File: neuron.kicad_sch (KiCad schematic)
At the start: 91 parts, among them J1 Conn_02x01, J2 Conn_02x01, J3 Conn_02x01, J4 Conn_02x03, Q1 2sk3018, Q10 2sk3018, Q11 2sk3018, Q12 2sk3018, Q2 2sk3018, Q3 2sk3018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

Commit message: Replace synaptic time constant and weight potentiometers by 22k
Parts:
- RV1, RV2, RV3: value 5k -> 22k; LCSC C128557 -> C128552
- RV4: value 20k -> 22k; LCSC C128550 -> C128552
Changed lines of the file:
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@@
       (effects (font (size 1.27 1.27)))
     )
-    (property "Value" "5k" (at 73.66 204.47 90)
+    (property "Value" "22k" (at 73.66 204.47 90)
       (effects (font (size 1.27 1.27)))
     )
@@
       (effects (font (size 1.27 1.27)) hide)
     )
-    (property "LCSC" "C128557" (at 73.66 198.12 0)
+    (property "LCSC" "C128552" (at 73.66 198.12 0)
       (effects (font (size 1.27 1.27)) hide)
     )
@@
       (effects (font (size 1.27 1.27)))
     )
-    (property "Value" "5k" (at 73.66 66.04 90)
+    (property "Value" "22k" (at 73.66 66.04 90)
       (effects (font (size 1.27 1.27)))
     )
@@
       (effects (font (size 1.27 1.27)) hide)
     )
-    (property "LCSC" "C128557" (at 73.66 59.69 0)
+    (property "LCSC" "C128552" (at 73.66 59.69 0)
       (effects (font (size 1.27 1.27)) hide)
     )
@@
       (effects (font (size 1.27 1.27)))
     )
-    (property "Value" "5k" (at 73.66 135.89 90)
+    (property "Value" "22k" (at 73.66 135.89 90)
       (effects (font (size 1.27 1.27)))
     )
@@
       (effects (font (size 1.27 1.27)) hide)
     )
-    (property "LCSC" "C128557" (at 73.66 129.54 0)
+    (property "LCSC" "C128552" (at 73.66 129.54 0)
       (effects (font (size 1.27 1.27)) hide)
     )
@@
       (effects (font (size 1.27 1.27)) (justify right))
     )
-    (property "Value" "20k" (at 125.73 85.725 0)
+    (property "Value" "22k" (at 125.73 85.725 0)
       (effects (font (size 1.27 1.27)) (justify right))
     )
@@
       (effects (font (size 1.27 1.27)) hide)
     )
-    (property "LCSC" "C128550" (at 127.635 83.185 0)
+    (property "LCSC" "C128552" (at 127.635 83.185 0)
       (effects (font (size 1.27 1.27)) hide)
     )

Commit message: Replace membrane capacitor by more common part
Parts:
- C5: LCSC C2836678 -> C415703
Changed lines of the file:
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@@
       (effects (font (size 1.27 1.27)) hide)
     )
-    (property "LCSC" "C2836678" (at 232.41 98.425 0)
+    (property "LCSC" "C415703" (at 232.41 98.425 0)
       (effects (font (size 1.27 1.27)) hide)
     )

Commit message: Replace LEDs by more yellow one
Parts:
- D1, D2, D3, D4, D5, D6, D7: LCSC C779448 -> C965792
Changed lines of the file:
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@@
       (effects (font (size 1.27 1.27)) hide)
     )
-    (property "LCSC" "C779448" (at 401.32 104.775 0)
+    (property "LCSC" "C965792" (at 401.32 104.775 0)
       (effects (font (size 1.27 1.27)) hide)
     )
@@
       (effects (font (size 1.27 1.27)) hide)
     )
-    (property "LCSC" "C779448" (at 401.32 117.475 0)
+    (property "LCSC" "C965792" (at 401.32 117.475 0)
       (effects (font (size 1.27 1.27)) hide)
     )
@@
       (effects (font (size 1.27 1.27)) hide)
     )
-    (property "LCSC" "C779448" (at 401.32 66.675 0)
+    (property "LCSC" "C965792" (at 401.32 66.675 0)
       (effects (font (size 1.27 1.27)) hide)
     )
@@
       (effects (font (size 1.27 1.27)) hide)
     )
-    (property "LCSC" "C779448" (at 401.32 130.175 0)
+    (property "LCSC" "C965792" (at 401.32 130.175 0)
       (effects (font (size 1.27 1.27)) hide)
     )
@@
       (effects (font (size 1.27 1.27)) hide)
     )
-    (property "LCSC" "C779448" (at 401.32 92.075 0)
+    (property "LCSC" "C965792" (at 401.32 92.075 0)
       (effects (font (size 1.27 1.27)) hide)
     )
@@
       (effects (font (size 1.27 1.27)) hide)
     )
-    (property "LCSC" "C779448" (at 400.05 151.13 0)
+    (property "LCSC" "C965792" (at 400.05 151.13 0)
       (effects (font (size 1.27 1.27)) hide)
     )
@@
       (effects (font (size 1.27 1.27)) hide)
     )
-    (property "LCSC" "C779448" (at 401.32 79.375 0)
-      (effects (font (size 1.27 1.27)) hide)
-    )
+    (property "LCSC" "C965792" (at 401.32 79.375 0)
+      (effects (font (size 1.27 1.27)) hide)
+    )

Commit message: Change LEDs due to stock shortages
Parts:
- D1, D2, D3, D4, D5, D6, D7: LCSC C965792 -> C779450
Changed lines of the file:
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@@
       (effects (font (size 1.27 1.27)) hide)
     )
-    (property "LCSC" "C965792" (at 401.32 104.775 0)
+    (property "LCSC" "C779450" (at 401.32 104.775 0)
       (effects (font (size 1.27 1.27)) hide)
     )
@@
       (effects (font (size 1.27 1.27)) hide)
     )
-    (property "LCSC" "C965792" (at 401.32 117.475 0)
+    (property "LCSC" "C779450" (at 401.32 117.475 0)
       (effects (font (size 1.27 1.27)) hide)
     )
@@
       (effects (font (size 1.27 1.27)) hide)
     )
-    (property "LCSC" "C965792" (at 401.32 66.675 0)
+    (property "LCSC" "C779450" (at 401.32 66.675 0)
       (effects (font (size 1.27 1.27)) hide)
     )
@@
       (effects (font (size 1.27 1.27)) hide)
     )
-    (property "LCSC" "C965792" (at 401.32 130.175 0)
+    (property "LCSC" "C779450" (at 401.32 130.175 0)
       (effects (font (size 1.27 1.27)) hide)
     )
@@
       (effects (font (size 1.27 1.27)) hide)
     )
-    (property "LCSC" "C965792" (at 401.32 92.075 0)
+    (property "LCSC" "C779450" (at 401.32 92.075 0)
       (effects (font (size 1.27 1.27)) hide)
     )
@@
       (effects (font (size 1.27 1.27)) hide)
     )
-    (property "LCSC" "C965792" (at 400.05 151.13 0)
+    (property "LCSC" "C779450" (at 400.05 151.13 0)
       (effects (font (size 1.27 1.27)) hide)
     )
@@
       (effects (font (size 1.27 1.27)) hide)
     )
-    (property "LCSC" "C965792" (at 401.32 79.375 0)
-      (effects (font (size 1.27 1.27)) hide)
-    )
+    (property "LCSC" "C779450" (at 401.32 79.375 0)
+      (effects (font (size 1.27 1.27)) hide)
+    )

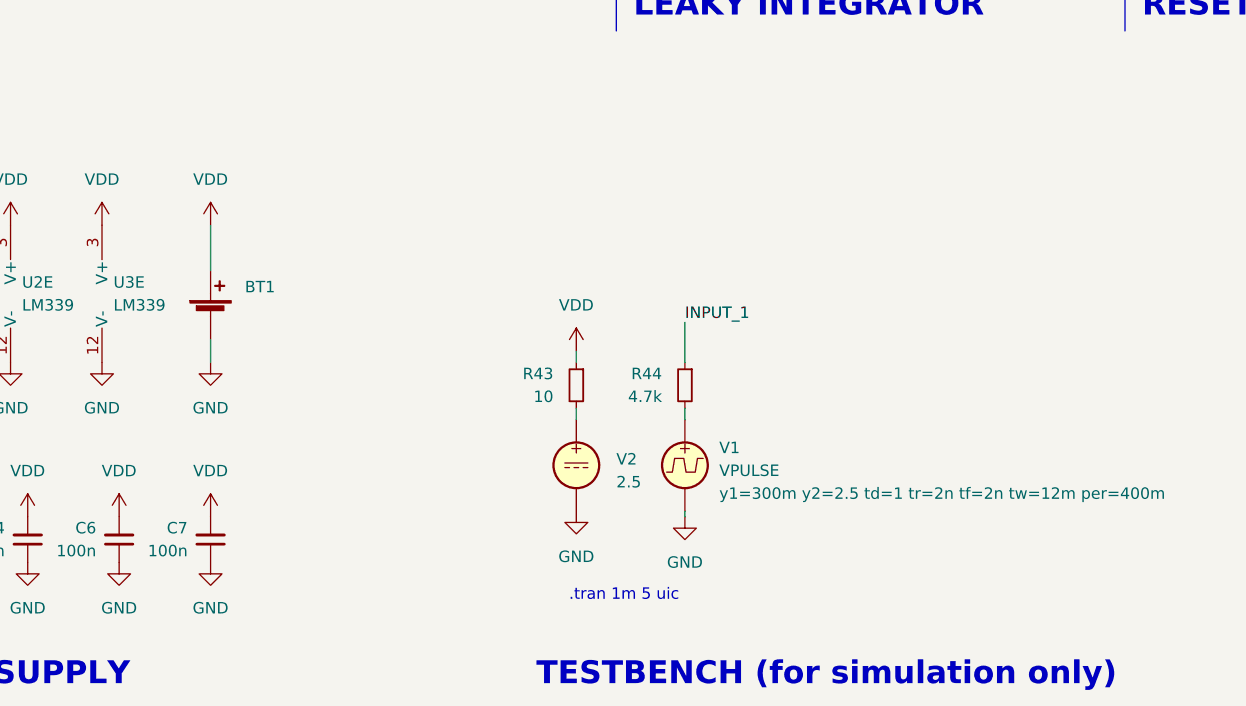
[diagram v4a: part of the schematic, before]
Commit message: Add (optional) power switch on back side
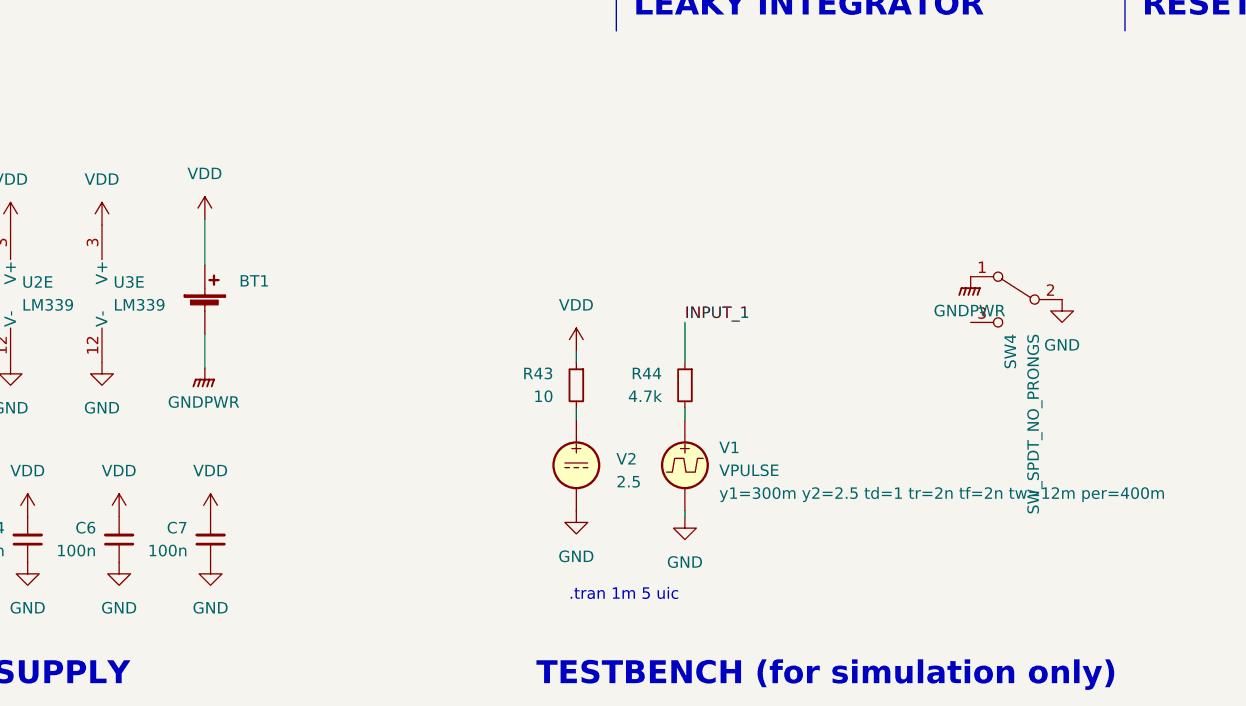
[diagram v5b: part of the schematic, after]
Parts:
- added SW4: SW_SPDT_NO_PRONGS, Custom:SSAJ120100, symbol Switch:SW_SPDT
- SW1, SW2, SW3: footprint Custom:K3-1290S-E1 -> Custom:K3-1296S-E1; LCSC C145854 -> C128955
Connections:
- net GND: now also SW4.2 (B); no longer BT1.2 (-)
- new net GNDPWR: BT1.2 (-), SW4.1 (A)
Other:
- moved on the sheet: BT1
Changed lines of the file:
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@@
     (stroke (width 0) (type default))
   )
-  (wire (pts (xy 167.005 212.725) (xy 167.005 215.265))
-    (stroke (width 0) (type default))
-  )
   (wire (pts (xy 63.5 113.03) (xy 63.5 116.84))
     (stroke (width 0) (type default))
@@
     (stroke (width 0) (type default))
   )
-  (wire (pts (xy 167.005 200.025) (xy 167.005 205.105))
+  (wire (pts (xy 166.37 199.39) (xy 166.37 204.47))
     (stroke (width 0) (type default))
   )
@@
     (stroke (width 0) (type default))
   )
+  (wire (pts (xy 166.37 212.09) (xy 166.37 215.9))
+    (stroke (width 0) (type default))
+  )
   (wire (pts (xy 367.03 107.315) (xy 369.57 107.315))
     (stroke (width 0) (type default))
@@
     )
   )
-  (symbol (lib_id "power:VDD") (at 167.005 200.025 0) (unit 1)
+  (symbol (lib_id "power:VDD") (at 166.37 199.39 0) (unit 1)
     (in_bom yes) (on_board yes) (dnp no) (fields_autoplaced)
-    (property "Reference" "#PWR023" (at 167.005 203.835 0)
+    (property "Reference" "#PWR023" (at 166.37 203.2 0)
       (effects (font (size 1.27 1.27)) hide)
     )
-    (property "Value" "VDD" (at 167.005 194.945 0)
+    (property "Value" "VDD" (at 166.37 194.31 0)
       (effects (font (size 1.27 1.27)))
     )
-    (property "Footprint" "" (at 167.005 200.025 0)
+    (property "Footprint" "" (at 166.37 199.39 0)
       (effects (font (size 1.27 1.27)) hide)
     )
-    (property "Datasheet" "" (at 167.005 200.025 0)
+    (property "Datasheet" "" (at 166.37 199.39 0)
       (effects (font (size 1.27 1.27)) hide)
     )
@@
       (effects (font (size 1.27 1.27)) (justify right))
     )
-    (property "Footprint" "Custom:K3-1290S-E1" (at 50.8 137.16 0)
+    (property "Footprint" "Custom:K3-1296S-E1" (at 50.8 137.16 0)
       (effects (font (size 1.27 1.27)) hide)
     )
@@
       (effects (font (size 1.27 1.27)) hide)
     )
-    (property "LCSC" "C145854" (at 50.8 137.16 0)
+    (property "LCSC" "C128955" (at 50.8 137.16 0)
       (effects (font (size 1.27 1.27)) hide)
     )
@@
     )
   )
+  (symbol (lib_id "power:GND") (at 261.62 208.28 0) (unit 1)
+    (in_bom yes) (on_board yes) (dnp no) (fields_autoplaced)
+    (property "Reference" "#PWR064" (at 261.62 214.63 0)
+      (effects (font (size 1.27 1.27)) hide)
+    )
+    (property "Value" "GND" (at 261.62 213.36 0)
+      (effects (font (size 1.27 1.27)))
+    )
+    (property "Footprint" "" (at 261.62 208.28 0)
+      (effects (font (size 1.27 1.27)) hide)
+    )
+    (property "Datasheet" "" (at 261.62 208.28 0)
+      (effects (font (size 1.27 1.27)) hide)
+    )
+    (pin "1")
+    (instances
+      (project "neuron"
+        (path "/ceb44bb3-3806-4f1d-b60c-2d4eb7174dea"
+          (reference "#PWR064") (unit 1)
+        )
+      )
+    )
+  )
   (symbol (lib_id "Device:C_Small") (at 337.185 115.57 0) (mirror y) (unit 1)
     (in_bom yes) (on_board yes) (dnp no)
@@
     )
   )
-  (symbol (lib_id "Device:Battery_Cell") (at 167.005 210.185 0) (unit 1)
+  (symbol (lib_id "Device:Battery_Cell") (at 166.37 209.55 0) (unit 1)
     (in_bom yes) (on_board yes) (dnp no) (fields_autoplaced)
-    (property "Reference" "BT1" (at 170.815 206.8829 0)
+    (property "Reference" "BT1" (at 170.18 206.2479 0)
       (effects (font (size 1.27 1.27)) (justify left))
     )
-    (property "Value" "type=\"R\" model=\"Battery_Cell\" lib=\"\"" (at 170.815 209.4229 0)
+    (property "Value" "type=\"R\" model=\"Battery_Cell\" lib=\"\"" (at 170.18 208.7879 0)
       (effects (font (size 1.27 1.27)) (justify left) hide)
     )
-    (property "Footprint" "Custom:CR2032_Holder" (at 167.005 208.661 90)
+    (property "Footprint" "Custom:CR2032_Holder" (at 166.37 208.026 90)
       (effects (font (size 1.27 1.27)) hide)
     )
-    (property "Datasheet" "~" (at 167.005 208.661 90)
+    (property "Datasheet" "~" (at 166.37 208.026 90)
       (effects (font (size 1.27 1.27)) hide)
     )
-    (property "LCSC" "C70377" (at 167.005 210.185 0)
+    (property "LCSC" "C70377" (at 166.37 209.55 0)
       (effects (font (size 1.27 1.27)) hide)
     )
-    (property "Sim.Enable" "0" (at 167.005 210.185 0)
+    (property "Sim.Enable" "0" (at 166.37 209.55 0)
       (effects (font (size 1.27 1.27)) hide)
     )
-    (property "Sim.Device" "SPICE" (at 167.005 210.185 0)
+    (property "Sim.Device" "SPICE" (at 166.37 209.55 0)
       (effects (font (size 1.27 1.27)) hide)
     )
-    (property "Sim.Params" "type=\"R\" model=\"Battery_Cell\" lib=\"\"" (at 73.025 29.845 0)
+    (property "Sim.Params" "type=\"R\" model=\"Battery_Cell\" lib=\"\"" (at 72.39 29.21 0)
       (effects (font (size 1.27 1.27)) hide)
     )
-    (property "Sim.Pins" "1=1 2=2" (at 73.025 29.845 0)
+    (property "Sim.Pins" "1=1 2=2" (at 72.39 29.21 0)
       (effects (font (size 1.27 1.27)) hide)
     )
@@
     )
   )
+  (symbol (lib_id "power:GNDPWR") (at 166.37 215.9 0) (unit 1)
+    (in_bom yes) (on_board yes) (dnp no) (fields_autoplaced)
+    (property "Reference" "#PWR063" (at 166.37 220.98 0)
+      (effects (font (size 1.27 1.27)) hide)
+    )
+    (property "Value" "GNDPWR" (at 166.243 219.71 0)
+      (effects (font (size 1.27 1.27)))
+    )
+    (property "Footprint" "" (at 166.37 217.17 0)
+      (effects (font (size 1.27 1.27)) hide)
+    )
+    (property "Datasheet" "" (at 166.37 217.17 0)
+      (effects (font (size 1.27 1.27)) hide)
+    )
+    (pin "1")
+    (instances
+      (project "neuron"
+        (path "/ceb44bb3-3806-4f1d-b60c-2d4eb7174dea"
+          (reference "#PWR063") (unit 1)
+        )
+      )
+    )
+  )
   (symbol (lib_id "Transistor_FET:2N7002") (at 188.595 111.125 0) (unit 1)
     (in_bom yes) (on_board yes) (dnp no)
@@
     )
   )
+  (symbol (lib_id "Switch:SW_SPDT") (at 256.54 208.28 0) (mirror y) (unit 1)
+    (in_bom yes) (on_board yes) (dnp no)
+    (property "Reference" "SW4" (at 255.905 212.09 90)
+      (effects (font (size 1.27 1.27)) (justify right))
+    )
+    (property "Value" "SW_SPDT_NO_PRONGS" (at 258.445 212.09 90)
+      (effects (font (size 1.27 1.27)) (justify right))
+    )
+    (property "Footprint" "Custom:SSAJ120100" (at 256.54 208.28 0)
+      (effects (font (size 1.27 1.27)) hide)
+    )
+    (property "Datasheet" "~" (at 256.54 208.28 0)
+      (effects (font (size 1.27 1.27)) hide)
+    )
+    (property "LCSC" "C160864" (at 256.54 208.28 0)
+      (effects (font (size 1.27 1.27)) hide)
+    )
+    (property "Field5" "" (at 256.54 208.28 0)
+      (effects (font (size 1.27 1.27)) hide)
+    )
+    (property "Sim.Library" "models/static_switch.mod" (at 256.54 208.28 0)
+      (effects (font (size 1.27 1.27)) hide)
+    )
+    (property "Sim.Name" "switch" (at 256.54 208.28 0)
+      (effects (font (size 1.27 1.27)) hide)
+    )
+    (property "Sim.Device" "SUBCKT" (at 256.54 208.28 0)
+      (effects (font (size 1.27 1.27)) hide)
+    )
+    (property "Sim.Pins" "1=1 2=2 3=3" (at 256.54 208.28 0)
+      (effects (font (size 1.27 1.27)) hide)
+    )
+    (pin "1")
+    (pin "2")
+    (pin "3")
+    (instances
+      (project "neuron"
+        (path "/ceb44bb3-3806-4f1d-b60c-2d4eb7174dea"
+          (reference "SW4") (unit 1)
+        )
+      )
+    )
+  )
   (symbol (lib_id "power:GND") (at 103.505 66.675 0) (mirror y) (unit 1)
     (in_bom yes) (on_board yes) (dnp no) (fields_autoplaced)
@@
       (effects (font (size 1.27 1.27)) (justify right))
     )
-    (property "Footprint" "Custom:K3-1290S-E1" (at 50.8 205.74 0)
+    (property "Footprint" "Custom:K3-1296S-E1" (at 50.8 205.74 0)
       (effects (font (size 1.27 1.27)) hide)
     )
@@
       (effects (font (size 1.27 1.27)) hide)
     )
-    (property "LCSC" "C145854" (at 50.8 205.74 0)
+    (property "LCSC" "C128955" (at 50.8 205.74 0)
       (effects (font (size 1.27 1.27)) hide)
     )
@@
       (effects (font (size 1.27 1.27)) (justify right))
     )
-    (property "Footprint" "Custom:K3-1290S-E1" (at 50.8 67.31 0)
+    (property "Footprint" "Custom:K3-1296S-E1" (at 50.8 67.31 0)
       (effects (font (size 1.27 1.27)) hide)
     )
@@
       (effects (font (size 1.27 1.27)) hide)
     )
-    (property "LCSC" "C145854" (at 50.8 67.31 0)
+    (property "LCSC" "C128955" (at 50.8 67.31 0)
       (effects (font (size 1.27 1.27)) hide)
     )
@@
     )
   )
+  (symbol (lib_id "power:GNDPWR") (at 251.46 205.74 0) (unit 1)
+    (in_bom yes) (on_board yes) (dnp no) (fields_autoplaced)
+    (property "Reference" "#PWR024" (at 251.46 210.82 0)
+      (effects (font (size 1.27 1.27)) hide)
+    )
+    (property "Value" "GNDPWR" (at 251.333 209.55 0)
+      (effects (font (size 1.27 1.27)))
+    )
+    (property "Footprint" "" (at 251.46 207.01 0)
+      (effects (font (size 1.27 1.27)) hide)
+    )
+    (property "Datasheet" "" (at 251.46 207.01 0)
+      (effects (font (size 1.27 1.27)) hide)
+    )
+    (pin "1")
+    (instances
+      (project "neuron"
+        (path "/ceb44bb3-3806-4f1d-b60c-2d4eb7174dea"
+          (reference "#PWR024") (unit 1)
+        )
+      )
+    )
+  )
   (symbol (lib_id "Device:R_Potentiometer_Small") (at 256.54 99.06 0) (unit 1)
     (in_bom yes) (on_board yes) (dnp no) (fields_autoplaced)
@@
         )
       )
-    )
-  )
-  (symbol (lib_id "power:GND") (at 167.005 215.265 0) (unit 1)
-    (in_bom no) (on_board no) (dnp no) (fields_autoplaced)
-    (property "Reference" "#PWR024" (at 167.005 221.615 0)
-      (effects (font (size 1.27 1.27)) hide)
-    )
-    (property "Value" "GND" (at 167.005 220.345 0)
-      (effects (font (size 1.27 1.27)))
-    )
-    (property "Footprint" "" (at 167.005 215.265 0)
-      (effects (font (size 1.27 1.27)) hide)
-    )
-    (property "Datasheet" "" (at 167.005 215.265 0)
-      (effects (font (size 1.27 1.27)) hide)
-    )
-    (pin "1")
-    (instances
-      (project "neuron"
-        (path "/ceb44bb3-3806-4f1d-b60c-2d4eb7174dea"
-          (reference "#PWR024") (unit 1)
-        )
-      )

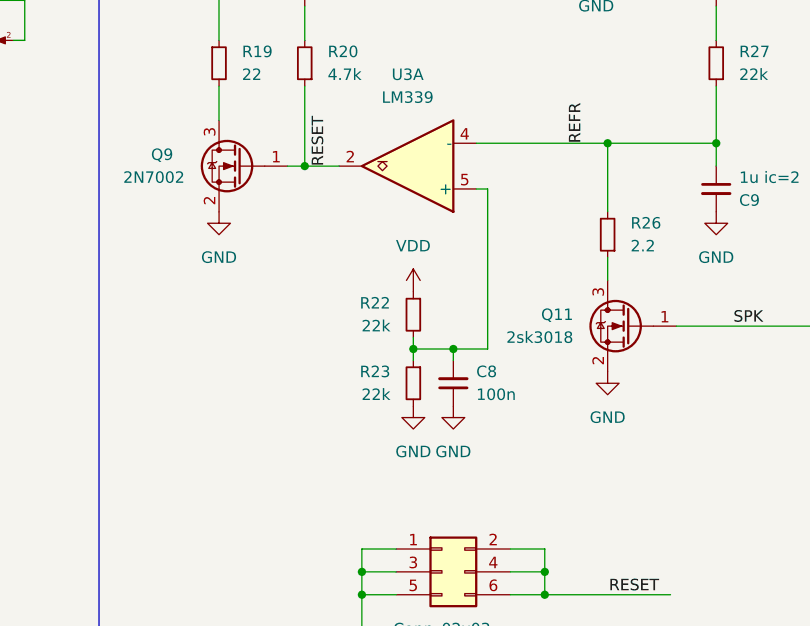
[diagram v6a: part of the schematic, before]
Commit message: Add hysteresis for refractory time comparator
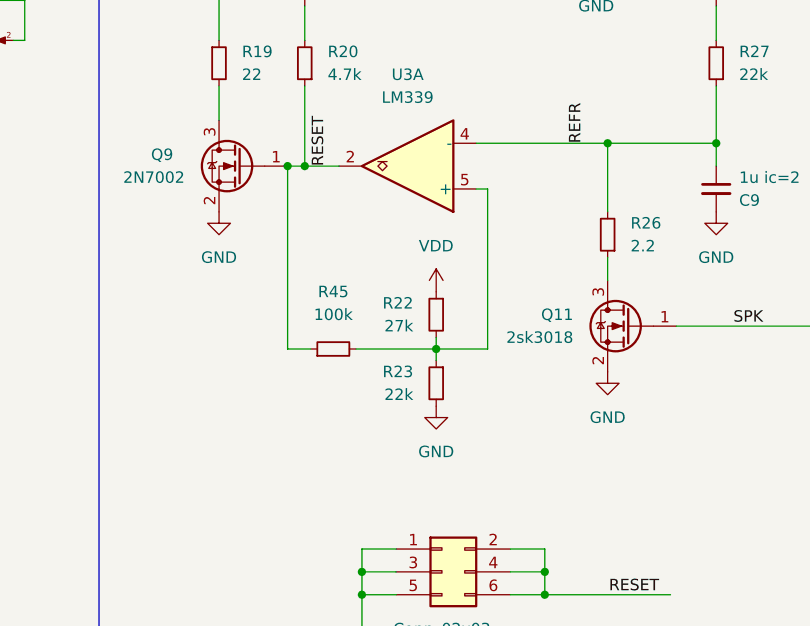
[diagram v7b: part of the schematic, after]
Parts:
- removed C8: 100n, Capacitor_SMD:C_0402_1005Metric, symbol Device:C_Small
- added R45: 100k, Resistor_SMD:R_0402_1005Metric, symbol Device:R_Small
- R22: value 22k -> 27k; LCSC C25768 -> C25771
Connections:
- net RESET: now also R45.1
- net at R22.2, R23.1, U3.5 (+): now also R45.2
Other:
- moved on the sheet: R22, R23
